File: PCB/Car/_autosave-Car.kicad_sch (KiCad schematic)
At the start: 12 parts, among them J1 L1, J10 FL2, J11 FLT, J2 L2, J3 R1, J4 R2, J5 R1+2, J6 L1+2, J7 Conn_01x03, J8 pi zero 2 w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

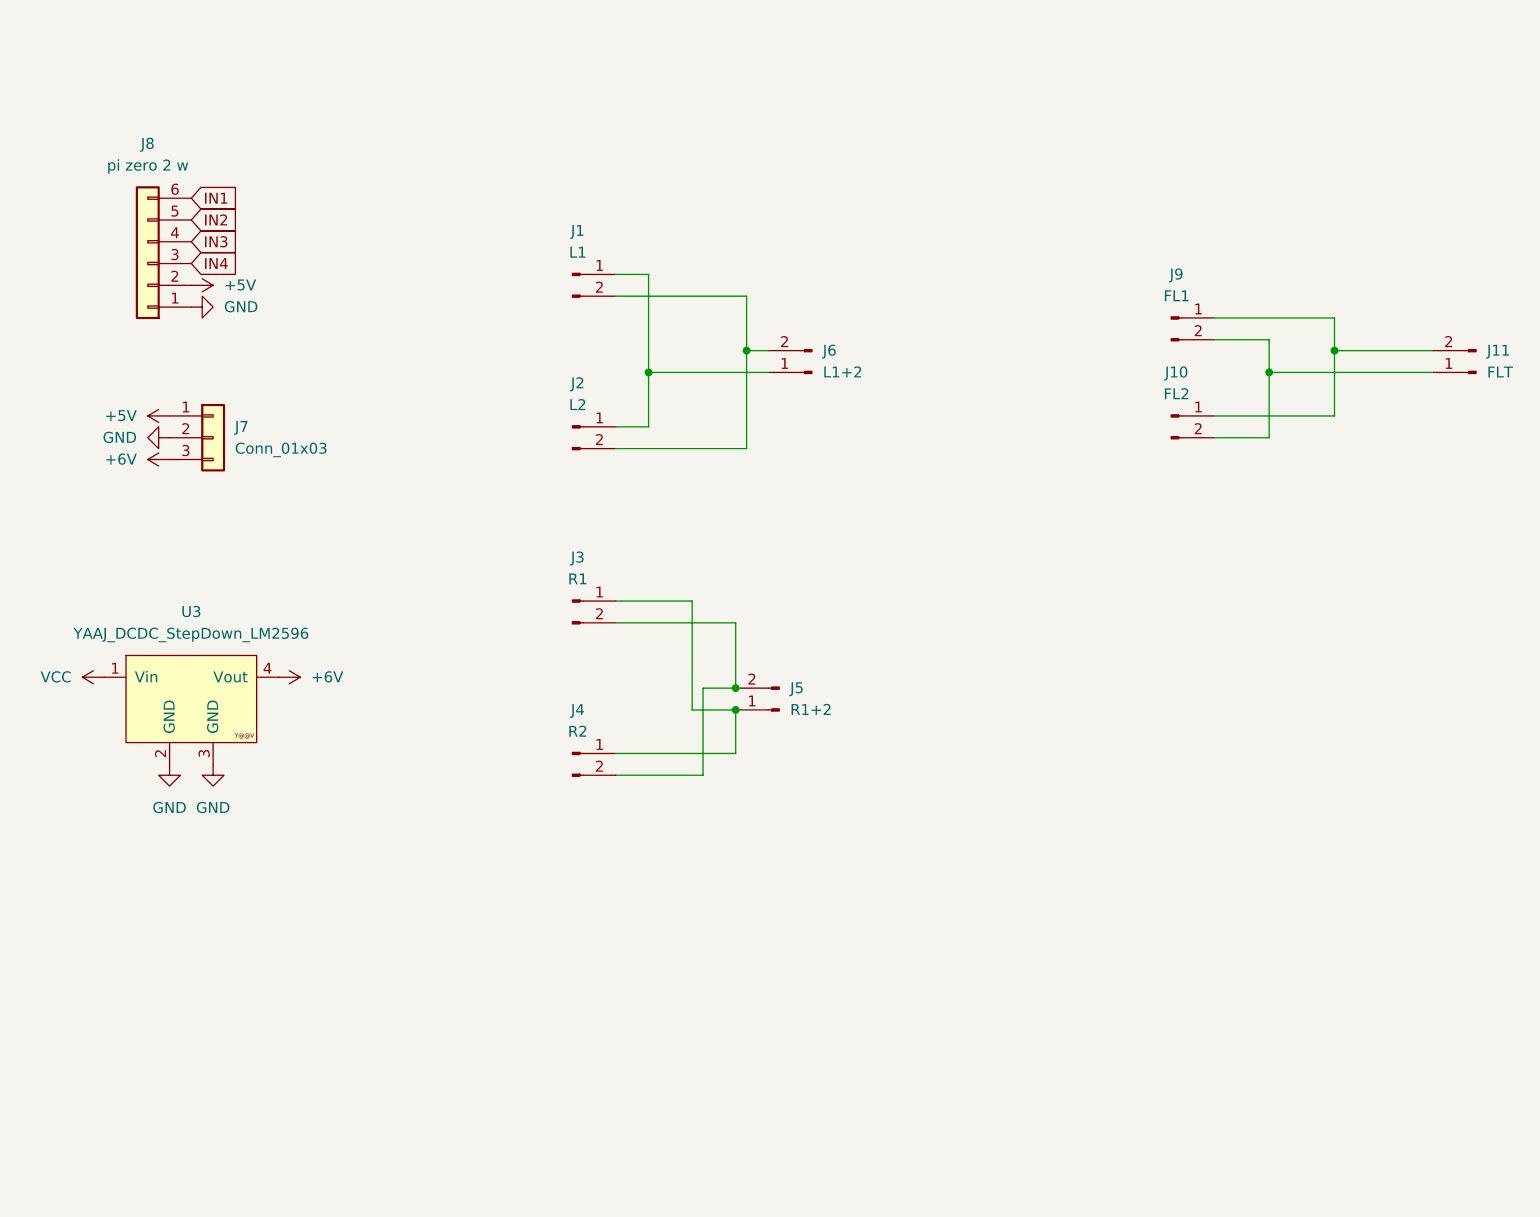
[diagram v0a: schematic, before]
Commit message: added firmware, updated pcb
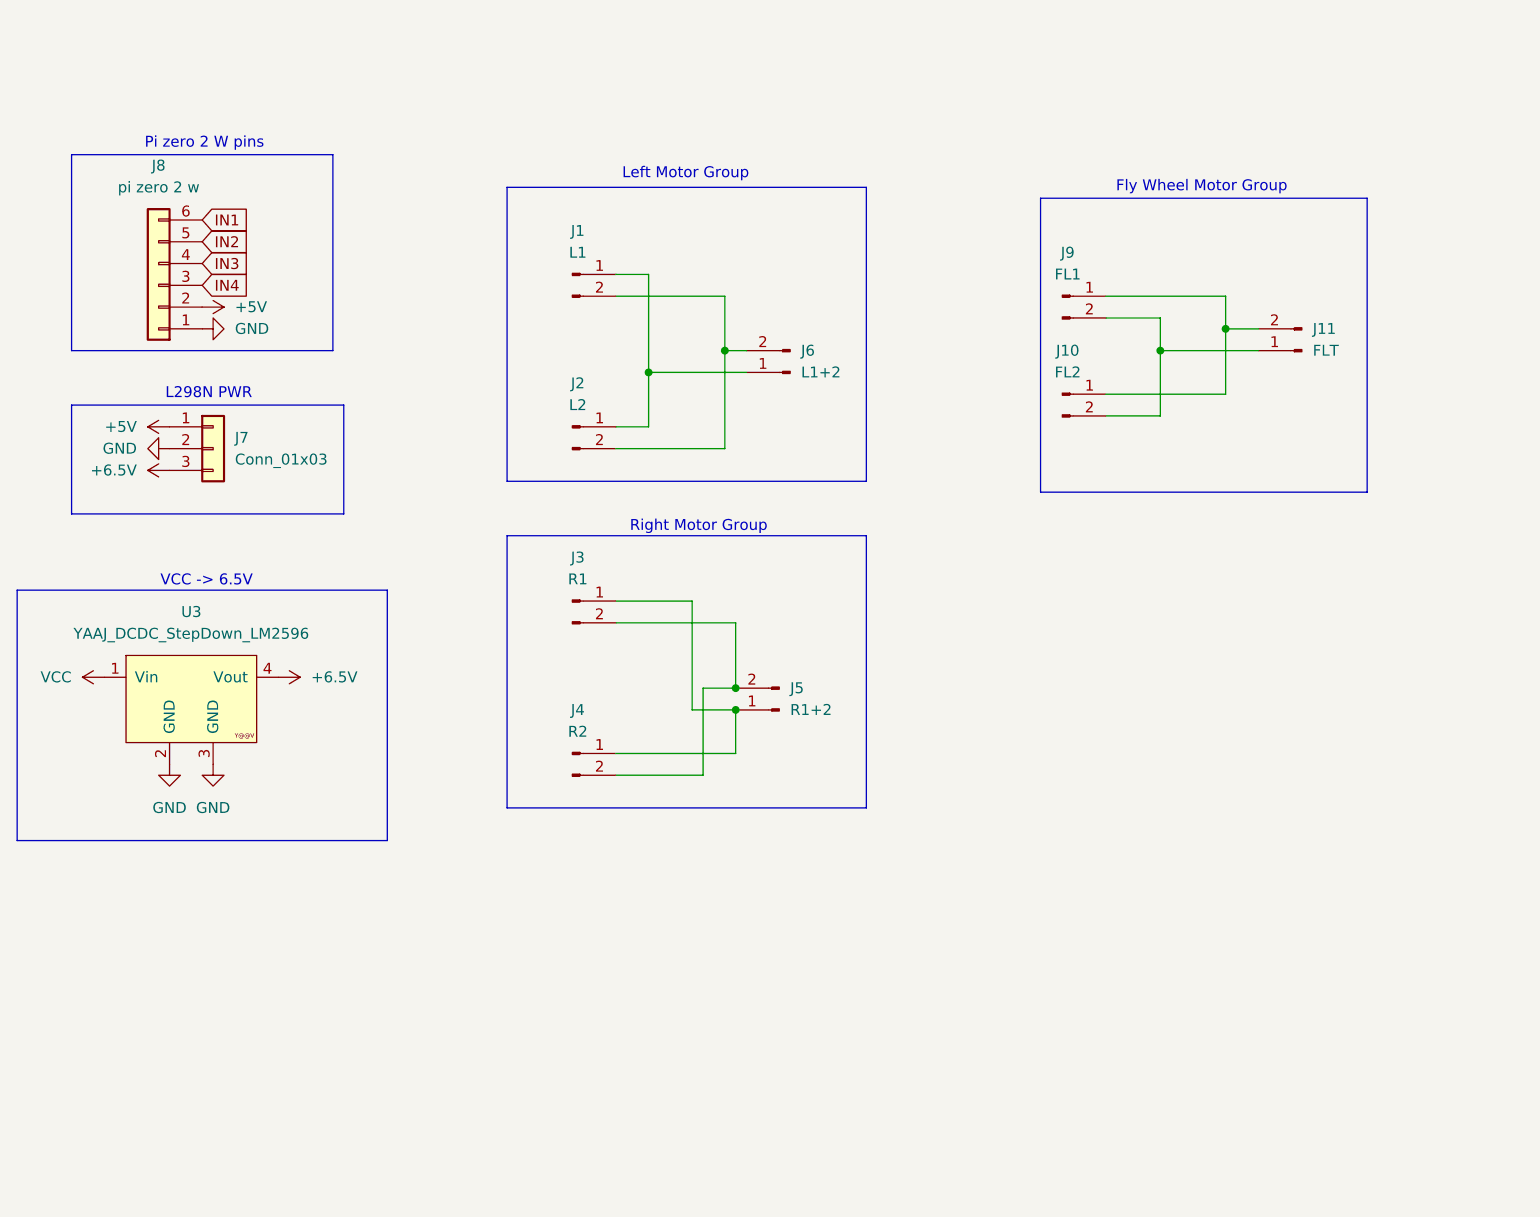
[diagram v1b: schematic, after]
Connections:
- net +6V renamed +6.5V
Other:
- note added: "Fly Wheel Motor Group"
- note added: "L298N PWR"
- note added: "Left Motor Group"
- note added: "Pi zero 2 W pins"
- note added: "Right Motor Group"
- note added: "VCC -> 6.5V"
- moved on the sheet: J10, J11, J6, J7, J8, J9

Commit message: updated CAD + PCB
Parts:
- added D1, D2: LED, LED_THT:LED_D5.0mm, symbol Device:LED
- added R1, R2: 220ohms, Resistor_THT:R_Axial_DIN0207_L6.3mm_D2.5mm_P7.62mm_Horizontal, symbol Device:R
- J1, J10, J11, J2, J3, J4, J5, J6, J9: footprint Connector_JST:JST_PH_S2B-PH-K_1x02_P2.00mm_Horizontal -> Connector:JWT_A3963_1x02_P3.96mm_Vertical
- J7: footprint Connector_JST:JST_PH_B3B-PH-K_1x03_P2.00mm_Vertical -> Connector:FanPinHeader_1x03_P2.54mm_Vertical
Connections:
- net GND: now also D1.2 (A), D2.2 (A)
- net at J10.2 (Pin_2), J9.2 (Pin_2): now also J11.2 (Pin_2); no longer J11.1 (Pin_1)
- net at J10.1 (Pin_1), J9.1 (Pin_1): now also J11.1 (Pin_1); no longer J11.2 (Pin_2)
- new net: D1.1 (K), R1.1
- new net: D2.1 (K), R2.1
- new net LED1: R1.2
- new net LED2: R2.2
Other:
- note added: "Fly Wheel Driver"
- note added: "LEDs"
- moved on the sheet: J8
